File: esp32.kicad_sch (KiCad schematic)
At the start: 10 parts, among them J2 Conn_01x06_Pin, SW1 BOOT, U6 ESP32-WROOM-32, U7 CMXT3904

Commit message: laid out stuff
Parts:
- added C16: 1uF, Capacitor_SMD:C_0805_2012Metric_Pad1.18x1.45mm_HandSolder, symbol Device:C
- added R28: 10K, Resistor_SMD:R_0805_2012Metric_Pad1.20x1.40mm_HandSolder, symbol Device:R
- C11: value 10uF -> 1uF
- J2: footprint Connector_PinSocket_2.54mm:PinSocket_1x06_P2.54mm_Vertical -> Connector_PinHeader_2.54mm:PinHeader_1x06_P2.54mm_Vertical
- U6: Availability Not in stock -> (none); Check_prices https://www.snapeda.com/parts/ESP32-WROOM-32/Espressif+Syst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 -> (none); MANUFACTURER Espressif Systems -> (none); MAXIMUM_PACKAGE_HEIGHT 3.2 mm -> (none); MF Espressif Systems -> (none); MP ESP32-WROOM-32 -> (none); PARTREV 2.9 -> (none); Package Non Standard Espressif Systems -> (none); Price None -> (none); STANDARD Manufacturer Recommendations -> (none); SnapEDA_Link https://www.snapeda.com/parts/ESP32-WROOM-32/Espressif+Syst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 -> (none)
- U7: Availability In Stock -> (none); Check_prices https://www.snapeda.com/parts/MBT3904DW1T1G/Onsemi/view-par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 -> (none); MF onsemi -> (none); MP MBT3904DW1T1G -> (none); Package SC-88-6 ON Semiconductor -> (none); Price None -> (none); Purchase-URL https://www.snapeda.com/api/url_track_click_mouser/?unipart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 -> (none); SnapEDA_Link https://www.snapeda.com/parts/MBT3904DW1T1G/Onsemi/view-par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 -> (none)
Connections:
- net +3.3V: now also R28.1
- net GND: now also C16.2
- net GPIO0: now also R28.2
- net LED_B: now also U6.31 (IO19); no longer U6.30 (IO18)
- net LED_G: now also U6.33 (IO21); no longer U6.28 (IO17)
- net LED_R: now also U6.36 (IO22); no longer U6.27 (IO16)
- net LED_W: now also U6.28 (IO17); no longer U6.31 (IO19)
- net RESETn: now also C16.1
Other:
- moved on the sheet: R12, R13, U7

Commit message: neat-ified schematics
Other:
- company: (none) -> The Art and Science of PCB Design
- title: (none) -> RGB LED Driver Demo Board
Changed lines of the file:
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@@
   (paper "USLetter")
   (title_block
+    (title "RGB LED Driver Demo Board")
     (date "2024-01-01")
     (rev "A01")
+    (company "The Art and Science of PCB Design")
   )
   (junction (at 90.17 57.15) (diameter 0) (color 0 0 0 0)

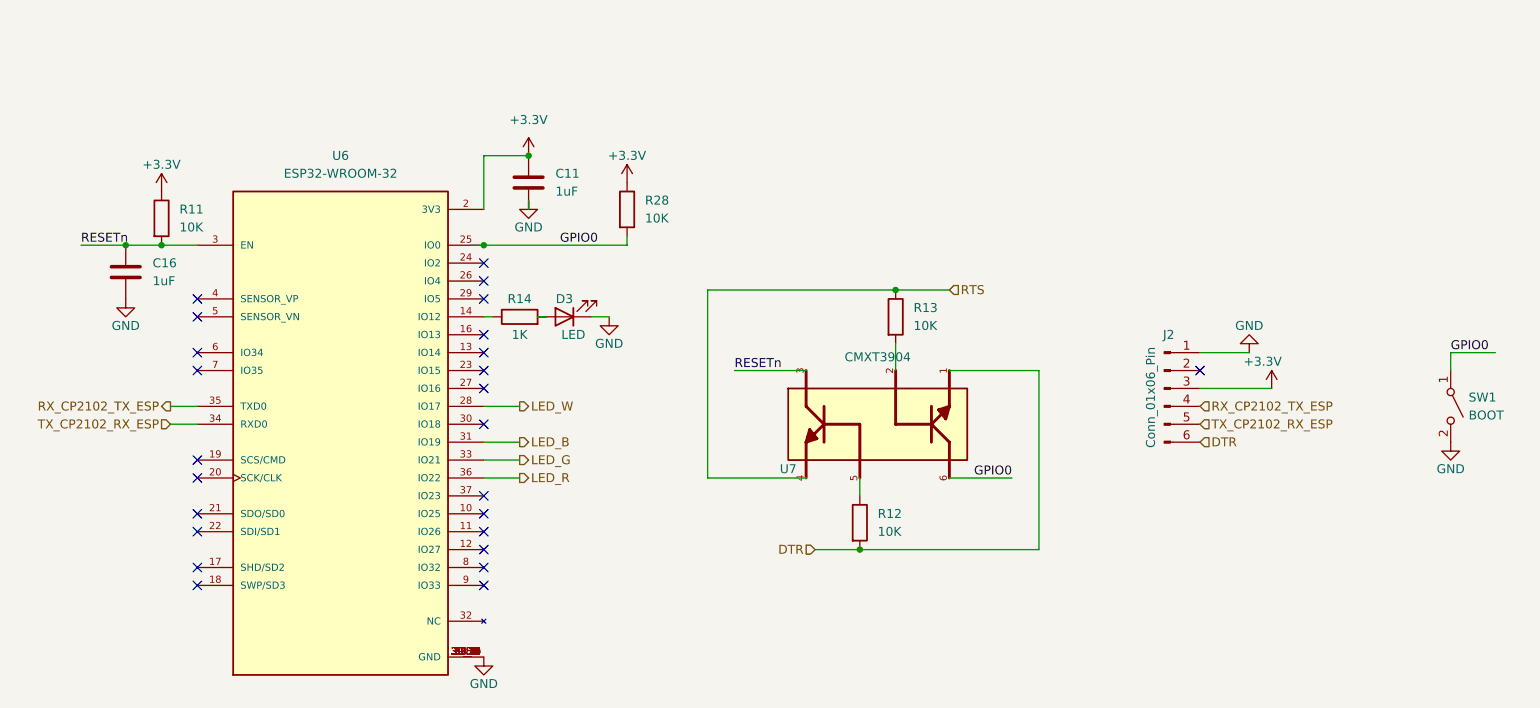
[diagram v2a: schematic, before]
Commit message: Added annotations, BOM count reduction
LED indicator resistors edited to save on BOM count

schematics made more neat, added some labels
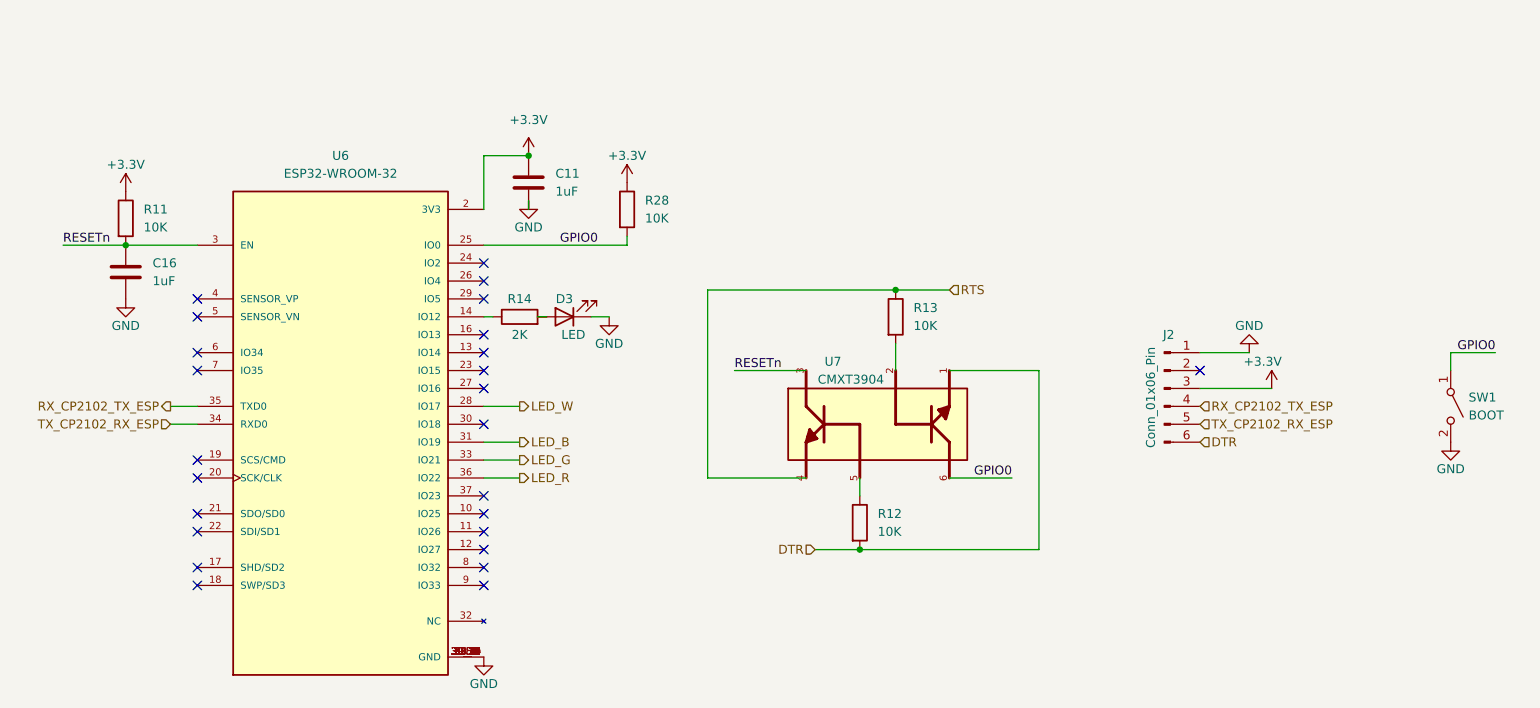
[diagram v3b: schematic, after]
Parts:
- R14: value 1K -> 2K
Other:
- moved on the sheet: R11
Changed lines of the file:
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@@
     (company "The Art and Science of PCB Design")
   )
-  (junction (at 90.17 57.15) (diameter 0) (color 0 0 0 0)
-  )
   (junction (at 39.37 57.15) (diameter 0) (color 0 0 0 0)
   )
   (junction (at 148.59 63.5) (diameter 0) (color 0 0 0 0)
-  )
-  (junction (at 44.45 57.15) (diameter 0) (color 0 0 0 0)
   )
   (junction (at 143.51 100.33) (diameter 0) (color 0 0 0 0)
@@
     (stroke (width 0) (type default))
   )
-  (wire (pts (xy 88.265 57.15) (xy 90.17 57.15))
-    (stroke (width 0) (type default))
-  )
   (wire (pts (xy 137.16 100.33) (xy 143.51 100.33))
     (stroke (width 0) (type default))
@@
     (stroke (width 0) (type default))
   )
-  (wire (pts (xy 39.37 57.15) (xy 44.45 57.15))
-    (stroke (width 0) (type default))
-  )
   (wire (pts (xy 198.755 72.39) (xy 191.77 72.39))
     (stroke (width 0) (type default))
@@
     (stroke (width 0) (type default))
   )
-  (wire (pts (xy 227.33 72.39) (xy 233.68 72.39))
-    (stroke (width 0) (type default))
-  )
   (wire (pts (xy 156.21 74.93) (xy 168.91 74.93))
     (stroke (width 0) (type default))
@@
     (stroke (width 0) (type default))
   )
-  (wire (pts (xy 227.33 74.93) (xy 227.33 72.39))
-    (stroke (width 0) (type default))
-  )
   (wire (pts (xy 168.91 74.93) (xy 168.91 100.33))
     (stroke (width 0) (type default))
@@
     (stroke (width 0) (type default))
   )
+  (wire (pts (xy 233.68 72.39) (xy 227.33 72.39))
+    (stroke (width 0) (type default))
+  )
+  (wire (pts (xy 39.37 57.15) (xy 49.53 57.15))
+    (stroke (width 0) (type default))
+  )
   (wire (pts (xy 121.92 63.5) (xy 148.59 63.5))
     (stroke (width 0) (type default))
   )
+  (wire (pts (xy 227.33 72.39) (xy 227.33 74.93))
+    (stroke (width 0) (type default))
+  )
   (wire (pts (xy 143.51 92.71) (xy 143.51 90.17))
     (stroke (width 0) (type default))
@@
     (stroke (width 0) (type default))
   )
-  (wire (pts (xy 44.45 57.15) (xy 49.53 57.15))
-    (stroke (width 0) (type default))
-  )
   (wire (pts (xy 135.89 90.17) (xy 121.92 90.17))
     (stroke (width 0) (type default))
@@
     (stroke (width 0) (type default))
   )
-  (wire (pts (xy 33.02 57.15) (xy 39.37 57.15))
+  (wire (pts (xy 30.48 57.15) (xy 39.37 57.15))
     (stroke (width 0) (type default))
   )
@@
     (stroke (width 0) (type default))
   )
-  (label "GPIO0" (at 227.33 72.39 0) (fields_autoplaced)
-    (effects (font (size 1.27 1.27)) (justify left bottom))
-  )
-  (label "RESETn" (at 33.02 57.15 0) (fields_autoplaced)
+  (label "GPIO0" (at 233.68 72.39 180) (fields_autoplaced)
+    (effects (font (size 1.27 1.27)) (justify right bottom))
+  )
+  (label "RESETn" (at 30.48 57.15 0) (fields_autoplaced)
     (effects (font (size 1.27 1.27)) (justify left bottom))
   )
@@
     )
   )
-  (symbol (lib_id "Device:R") (at 44.45 53.34 0) (unit 1)
-    (in_bom yes) (on_board yes) (dnp no) (fields_autoplaced)
-    (property "Reference" "R11" (at 46.99 52.07 0)
-      (effects (font (size 1.27 1.27)) (justify left))
-    )
-    (property "Value" "10K" (at 46.99 54.61 0)
-      (effects (font (size 1.27 1.27)) (justify left))
-    )
-    (property "Footprint" "Resistor_SMD:R_0805_2012Metric_Pad1.20x1.40mm_HandSolder" (at 42.672 53.34 90)
-      (effects (font (size 1.27 1.27)) hide)
-    )
-    (property "Datasheet" "~" (at 44.45 53.34 0)
-      (effects (font (size 1.27 1.27)) hide)
-    )
-    (property "Digikey PN" "" (at 44.45 53.34 0)
+  (symbol (lib_id "Device:R") (at 39.37 53.34 0) (unit 1)
+    (in_bom yes) (on_board yes) (dnp no) (fields_autoplaced)
+    (property "Reference" "R11" (at 41.91 52.07 0)
+      (effects (font (size 1.27 1.27)) (justify left))
+    )
+    (property "Value" "10K" (at 41.91 54.61 0)
+      (effects (font (size 1.27 1.27)) (justify left))
+    )
+    (property "Footprint" "Resistor_SMD:R_0805_2012Metric_Pad1.20x1.40mm_HandSolder" (at 37.592 53.34 90)
+      (effects (font (size 1.27 1.27)) hide)
+    )
+    (property "Datasheet" "~" (at 39.37 53.34 0)
+      (effects (font (size 1.27 1.27)) hide)
+    )
+    (property "Digikey PN" "" (at 39.37 53.34 0)
       (effects (font (size 1.27 1.27)) hide)
     )
@@
       (effects (font (size 1.27 1.27)))
     )
-    (property "Value" "1K" (at 95.25 69.85 90)
+    (property "Value" "2K" (at 95.25 69.85 90)
       (effects (font (size 1.27 1.27)))
     )
@@
   (symbol (lib_id "MBT3904DW1T1G:MBT3904DW1T1G") (at 146.05 82.55 0) (unit 1)
     (in_bom yes) (on_board yes) (dnp no)
-    (property "Reference" "U7" (at 133.35 88.9 0)
-      (effects (font (size 1.27 1.27)))
-    )
-    (property "Value" "CMXT3904" (at 146.05 73.025 0)
+    (property "Reference" "U7" (at 139.7 73.66 0)
+      (effects (font (size 1.27 1.27)))
+    )
+    (property "Value" "CMXT3904" (at 142.24 76.2 0)
       (effects (font (size 1.27 1.27)))
     )
@@
     )
   )
-  (symbol (lib_id "power:+3.3V") (at 44.45 49.53 0) (unit 1)
-    (in_bom yes) (on_board yes) (dnp no)
-    (property "Reference" "#PWR022" (at 44.45 53.34 0)
-      (effects (font (size 1.27 1.27)) hide)
-    )
-    (property "Value" "+3.3V" (at 44.45 45.72 0)
-      (effects (font (size 1.27 1.27)))
-    )
-    (property "Footprint" "" (at 44.45 49.53 0)
-      (effects (font (size 1.27 1.27)) hide)
-    )
-    (property "Datasheet" "" (at 44.45 49.53 0)
-      (effects (font (size 1.27 1.27)) hide)
-    )
+  (symbol (lib_id "power:+3.3V") (at 39.37 49.53 0) (unit 1)
+    (in_bom yes) (on_board yes) (dnp no)
+    (property "Reference" "#PWR022" (at 39.37 53.34 0)
+      (effects (font (size 1.27 1.27)) hide)
+    )
+    (property "Value" "+3.3V" (at 39.37 45.72 0)
+      (effects (font (size 1.27 1.27)))
+    )
+    (property "Footprint" "" (at 39.37 49.53 0)
+      (effects (font (size 1.27 1.27)) hide)
+    )
+    (property "Datasheet" "" (at 39.37 49.53 0)
+      (effects (font (size 1.27 1.27)) hide)
+    )

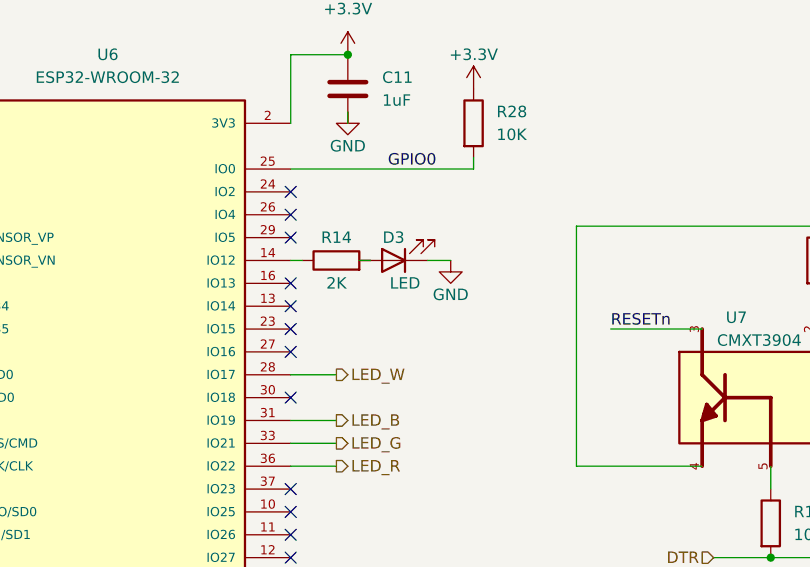
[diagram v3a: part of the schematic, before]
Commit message: added digikey PNs
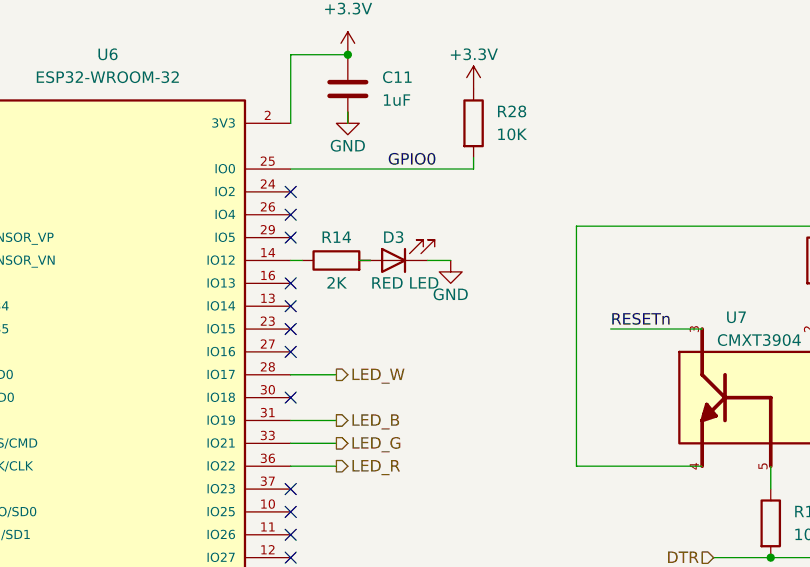
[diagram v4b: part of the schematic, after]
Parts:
- C11, C16: Digikey PN (none) -> 1276-1003-1-ND; MPN (none) -> CL21B104KBCNNNC
- D3: value LED -> RED LED; Digikey PN (none) -> 160-1427-1-ND; MPN (none) -> LTST-C171KRKT
- R11, R12, R13, R28: MPN (none) -> 0805W8F1002
- R14: MPN (none) -> 0805W8F2001
- SW1: Digikey PN (none) -> 450-1140-ND; MPN (none) -> FSMSM
- U6: Digikey PN (none) -> 1965-ESP32-WROOM-32E-N4CT-ND; MPN (none) -> ESP32-WROOM-32E-N4
- U7: Digikey PN (none) -> 1514-CMXT3904TRPBFREECT-ND; MPN (none) -> CMXT3904
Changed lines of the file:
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@@
+      (effects (font (size 1.27 1.27)) hide)
+    )
+    (property "MPN" "0805W8F1002" (at 39.37 53.34 0)
       (effects (font (size 1.27 1.27)) hide)
     )
@@
       (effects (font (size 1.27 1.27)) hide)
     )
-    (property "Digikey PN" "" (at 227.33 80.01 0)
+    (property "Digikey PN" "450-1140-ND" (at 227.33 80.01 0)
+      (effects (font (size 1.27 1.27)) hide)
+    )
+    (property "MPN" "FSMSM" (at 227.33 80.01 0)
       (effects (font (size 1.27 1.27)) hide)
     )
@@
       (effects (font (size 1.27 1.27)) hide)
     )
+    (property "MPN" "0805W8F1002" (at 143.51 96.52 0)
+      (effects (font (size 1.27 1.27)) hide)
+    )
     (pin "1")
     (pin "2")
@@
       (effects (font (size 1.27 1.27)) hide)
     )
+    (property "MPN" "0805W8F2001" (at 95.25 67.31 0)
+      (effects (font (size 1.27 1.27)) hide)
+    )
     (pin "1")
     (pin "2")
@@
       (effects (font (size 1.27 1.27)))
     )
-    (property "Value" "LED" (at 102.87 69.85 0)
+    (property "Value" "RED LED" (at 102.87 69.85 0)
       (effects (font (size 1.27 1.27)))
     )
@@
       (effects (font (size 1.27 1.27)) hide)
     )
-    (property "Digikey PN" "" (at 101.6 67.31 0)
+    (property "Digikey PN" "160-1427-1-ND" (at 101.6 67.31 0)
+      (effects (font (size 1.27 1.27)) hide)
+    )
+    (property "MPN" "LTST-C171KRKT" (at 101.6 67.31 0)
       (effects (font (size 1.27 1.27)) hide)
     )
@@
     )
     (property "Digikey PN" "" (at 110.49 52.07 0)
+      (effects (font (size 1.27 1.27)) hide)
+    )
+    (property "MPN" "0805W8F1002" (at 110.49 52.07 0)
       (effects (font (size 1.27 1.27)) hide)
     )
@@
       (effects (font (size 1.27 1.27)) hide)
     )
-    (property "Digikey PN" "" (at 69.85 85.09 0)
+    (property "Digikey PN" "1965-ESP32-WROOM-32E-N4CT-ND" (at 69.85 85.09 0)
+      (effects (font (size 1.27 1.27)) hide)
+    )
+    (property "MPN" "ESP32-WROOM-32E-N4" (at 69.85 85.09 0)
       (effects (font (size 1.27 1.27)) hide)
     )
@@
       (effects (font (size 1.27 1.27)) hide)
     )
-    (property "Digikey PN" "" (at 96.52 48.26 0)
+    (property "Digikey PN" "1276-1003-1-ND" (at 96.52 48.26 0)
+      (effects (font (size 1.27 1.27)) hide)
+    )
+    (property "MPN" "CL21B104KBCNNNC" (at 96.52 48.26 0)
       (effects (font (size 1.27 1.27)) hide)
     )
@@
       (effects (font (size 1.27 1.27)) hide)
     )
+    (property "MPN" "0805W8F1002" (at 148.59 67.31 0)
+      (effects (font (size 1.27 1.27)) hide)
+    )
     (pin "1")
     (pin "2")
@@
       (effects (font (size 1.27 1.27)) hide)
     )
-    (property "Digikey PN" "" (at 146.05 82.55 0)
+    (property "Digikey PN" "1514-CMXT3904TRPBFREECT-ND" (at 146.05 82.55 0)
+      (effects (font (size 1.27 1.27)) hide)
+    )
+    (property "MPN" "CMXT3904" (at 146.05 82.55 0)
       (effects (font (size 1.27 1.27)) hide)
     )
@@
       (effects (font (size 1.27 1.27)) hide)
     )
-    (property "Digikey PN" "" (at 39.37 60.96 0)
-      (effects (font (size 1.27 1.27)) hide)
-    )
+    (property "Digikey PN" "1276-1003-1-ND" (at 39.37 60.96 0)
+      (effects (font (size 1.27 1.27)) hide)
+    )
+    (property "MPN" "CL21B104KBCNNNC" (at 39.37 60.96 0)
+      (effects (font (size 1.27 1.27)) hide)
+    )

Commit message: added digikey PNs to all devices
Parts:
- R11, R12, R13, R28: Digikey PN (none) -> RMCF0805FT10K0CT-ND; MPN 0805W8F1002 -> RMCF0805FT10K0
- R14: Digikey PN (none) -> RMCF0805FT2K00CT-ND; MPN 0805W8F2001 -> RMCF0805FT2K00
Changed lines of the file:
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@@
       (effects (font (size 1.27 1.27)) hide)
     )
-    (property "Digikey PN" "" (at 39.37 53.34 0)
-      (effects (font (size 1.27 1.27)) hide)
-    )
-    (property "MPN" "0805W8F1002" (at 39.37 53.34 0)
+    (property "Digikey PN" "RMCF0805FT10K0CT-ND" (at 39.37 53.34 0)
+      (effects (font (size 1.27 1.27)) hide)
+    )
+    (property "MPN" "RMCF0805FT10K0" (at 39.37 53.34 0)
       (effects (font (size 1.27 1.27)) hide)
     )
@@
       (effects (font (size 1.27 1.27)) hide)
     )
-    (property "Digikey PN" "" (at 143.51 96.52 0)
-      (effects (font (size 1.27 1.27)) hide)
-    )
-    (property "MPN" "0805W8F1002" (at 143.51 96.52 0)
+    (property "Digikey PN" "RMCF0805FT10K0CT-ND" (at 143.51 96.52 0)
+      (effects (font (size 1.27 1.27)) hide)
+    )
+    (property "MPN" "RMCF0805FT10K0" (at 143.51 96.52 0)
       (effects (font (size 1.27 1.27)) hide)
     )
@@
       (effects (font (size 1.27 1.27)) hide)
     )
-    (property "Digikey PN" "" (at 95.25 67.31 0)
-      (effects (font (size 1.27 1.27)) hide)
-    )
-    (property "MPN" "0805W8F2001" (at 95.25 67.31 0)
+    (property "Digikey PN" "RMCF0805FT2K00CT-ND" (at 95.25 67.31 0)
+      (effects (font (size 1.27 1.27)) hide)
+    )
+    (property "MPN" "RMCF0805FT2K00" (at 95.25 67.31 0)
       (effects (font (size 1.27 1.27)) hide)
     )
@@
       (effects (font (size 1.27 1.27)) hide)
     )
-    (property "Digikey PN" "" (at 110.49 52.07 0)
-      (effects (font (size 1.27 1.27)) hide)
-    )
-    (property "MPN" "0805W8F1002" (at 110.49 52.07 0)
+    (property "Digikey PN" "RMCF0805FT10K0CT-ND" (at 110.49 52.07 0)
+      (effects (font (size 1.27 1.27)) hide)
+    )
+    (property "MPN" "RMCF0805FT10K0" (at 110.49 52.07 0)
       (effects (font (size 1.27 1.27)) hide)
     )
@@
       (effects (font (size 1.27 1.27)) hide)
     )
-    (property "Digikey PN" "" (at 148.59 67.31 0)
-      (effects (font (size 1.27 1.27)) hide)
-    )
-    (property "MPN" "0805W8F1002" (at 148.59 67.31 0)
-      (effects (font (size 1.27 1.27)) hide)
-    )
+    (property "Digikey PN" "RMCF0805FT10K0CT-ND" (at 148.59 67.31 0)
+      (effects (font (size 1.27 1.27)) hide)
+    )
+    (property "MPN" "RMCF0805FT10K0" (at 148.59 67.31 0)
+      (effects (font (size 1.27 1.27)) hide)
+    )
